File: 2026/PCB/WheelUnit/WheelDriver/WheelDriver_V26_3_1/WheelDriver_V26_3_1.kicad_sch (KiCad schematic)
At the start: 44 parts, among them J1 Conn_01x03_Socket, J10 Conn_01x04_Socket, J11 Conn_01x04_Socket, J12 Conn_01x04_Socket, J13 Conn_01x04_Socket, J14 Conn_01x06_Socket, J15 Conn_01x03_Socket, J16 Conn_01x03_Socket, J2 Conn_01x03_Socket, J9 Debug

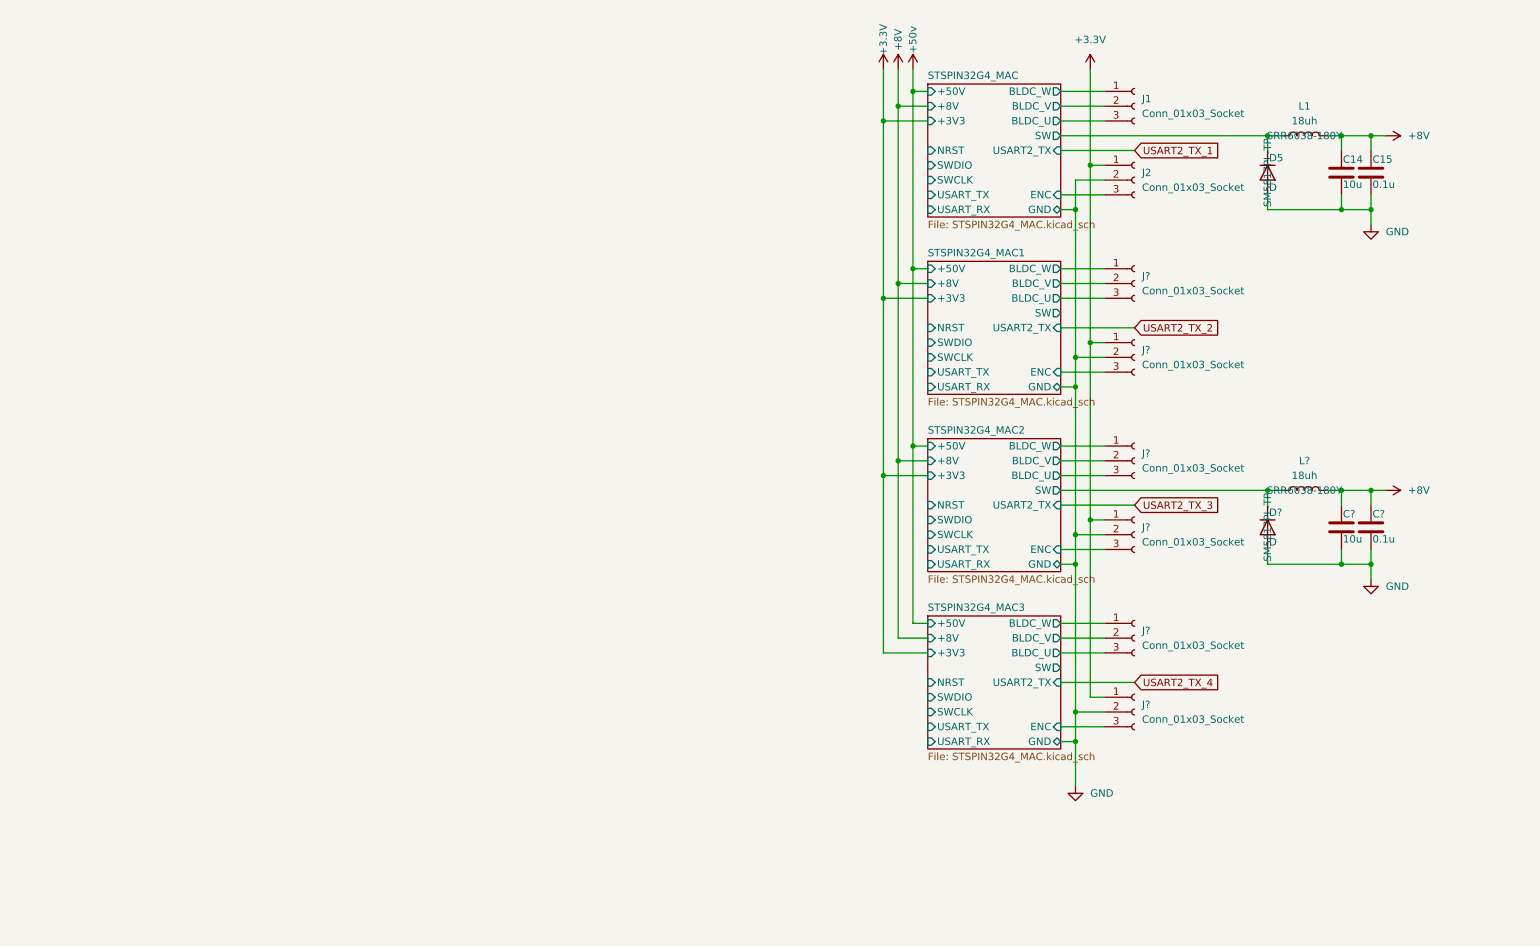
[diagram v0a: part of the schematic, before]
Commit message: 書き込み系統のバス追加
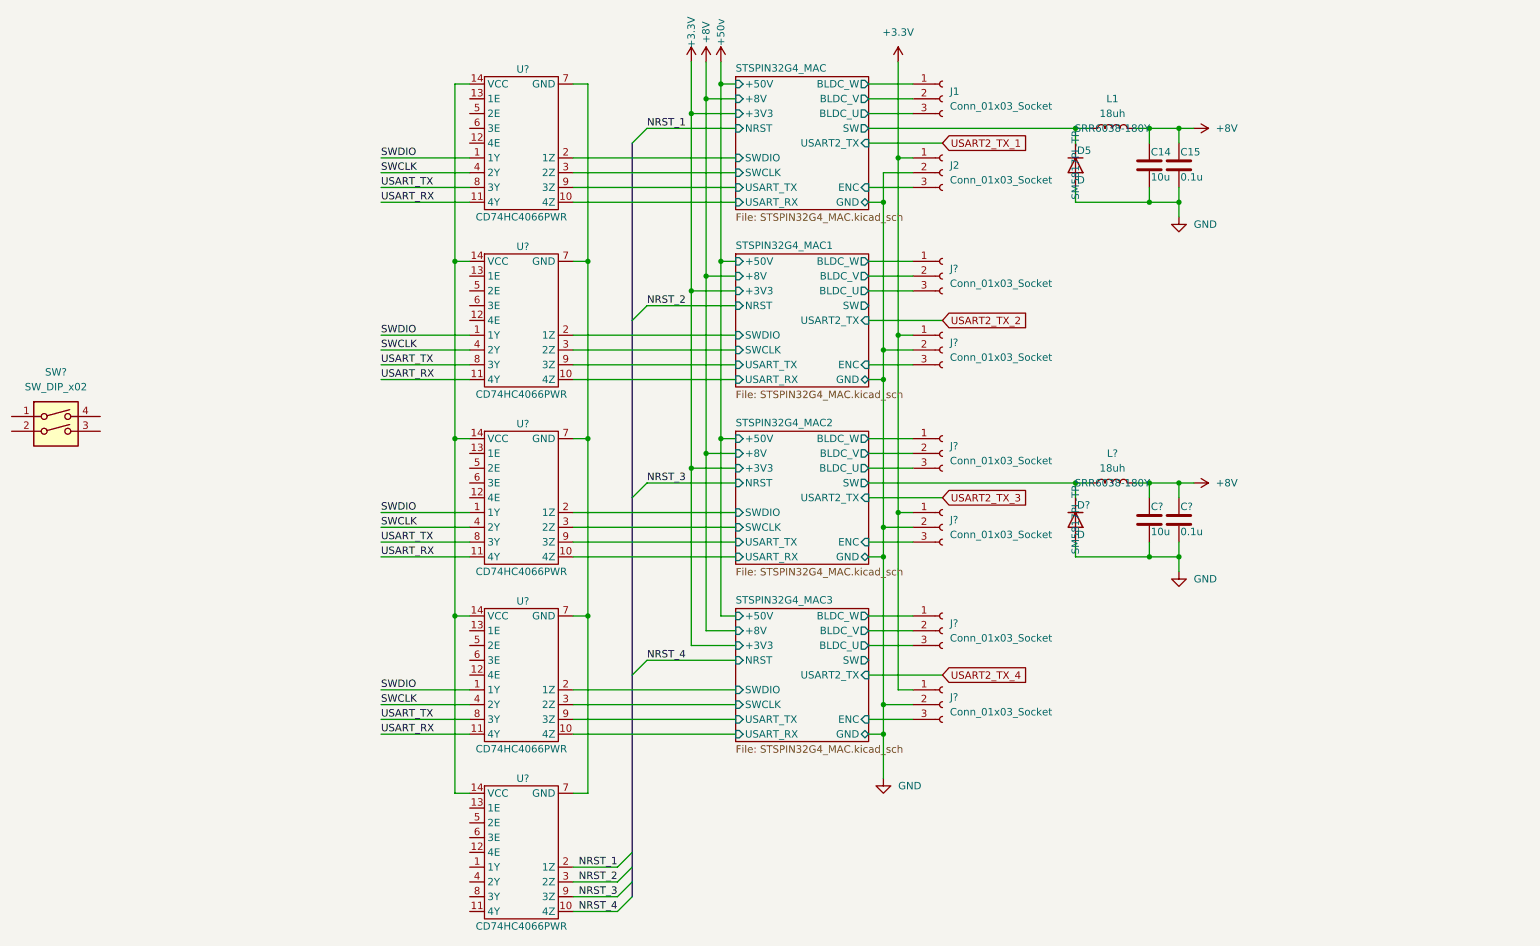
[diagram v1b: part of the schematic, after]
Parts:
- added SW?: SW_DIP_x02, symbol Switch:SW_DIP_x02
- added U? (x5): CD74HC4066PWR, symbol WheelUnit_LIB_SYM:CD74HC4066PWR
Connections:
- net STSPIN32G4_MAC/SWCLK: now also U?.3 (2Z)
- net STSPIN32G4_MAC/SWDIO: now also U?.2 (1Z)
- net STSPIN32G4_MAC/USART_RX: now also U?.10 (4Z)
- net STSPIN32G4_MAC/USART_TX: now also U?.9 (3Z)
- net STSPIN32G4_MAC1/SWCLK: now also U?.3 (2Z)
- net STSPIN32G4_MAC1/SWDIO: now also U?.2 (1Z)
- net STSPIN32G4_MAC1/USART_RX: now also U?.10 (4Z)
- net STSPIN32G4_MAC1/USART_TX: now also U?.9 (3Z)
- net STSPIN32G4_MAC2/SWCLK: now also U?.3 (2Z)
- net STSPIN32G4_MAC2/SWDIO: now also U?.2 (1Z)
- net STSPIN32G4_MAC2/USART_RX: now also U?.10 (4Z)
- net STSPIN32G4_MAC2/USART_TX: now also U?.9 (3Z)
- net STSPIN32G4_MAC3/SWCLK: now also U?.3 (2Z)
- net STSPIN32G4_MAC3/SWDIO: now also U?.2 (1Z)
- net STSPIN32G4_MAC3/USART_RX: now also U?.10 (4Z)
- net STSPIN32G4_MAC3/USART_TX: now also U?.9 (3Z)
- net SWCLK: now also U?.4 (2Y), U?.4 (2Y), U?.4 (2Y), U?.4 (2Y)
- net SWDIO: now also U?.1 (1Y), U?.1 (1Y), U?.1 (1Y), U?.1 (1Y)
- new net: U?.14 (VCC), U?.14 (VCC), U?.14 (VCC), U?.14 (VCC), U?.14 (VCC)
- new net: U?.7 (GND), U?.7 (GND), U?.7 (GND), U?.7 (GND), U?.7 (GND)
- new net NRST_1: U?.2 (1Z)
- new net NRST_2: U?.3 (2Z)
- new net NRST_3: U?.9 (3Z)
- new net NRST_4: U?.10 (4Z)
- new net USART_RX: U?.11 (4Y), U?.11 (4Y), U?.11 (4Y), U?.11 (4Y)
- new net USART_TX: U?.8 (3Y), U?.8 (3Y), U?.8 (3Y), U?.8 (3Y)
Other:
- moved on the sheet: C14, C15, C?, D5, D?, J1, J2, J?, L1, L?

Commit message: スイッチングの配線終わり
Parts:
- removed J14: Conn_01x06_Socket, Connector_JST:JST_PH_S6B-PH-K_1x06_P2.00mm_Horizontal, symbol Connector:Conn_01x06_Socket
- removed J9: Debug, Connector_JST:JST_PH_S7B-PH-K_1x07_P2.00mm_Horizontal, symbol Connector:Conn_01x07_Pin
- added J3: Conn_01x07_Pin, symbol Connector:Conn_01x07_Pin
- added J4: Conn_01x06_Pin, symbol Connector:Conn_01x06_Pin
- added SW1: SW_DIP_x02, symbol Switch:SW_DIP_x02
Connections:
- net +3.3V: now also J3.6 (Pin_6)
- net GND: now also J3.7 (Pin_7), J4.6 (Pin_6)
- net NRST: now also U?.1 (1Y), U?.11 (4Y), U?.4 (2Y), U?.8 (3Y), J3.3 (Pin_3)
- net SWCLK: now also J3.4 (Pin_4)
- net SWDIO: now also J3.5 (Pin_5)
- net USART2_RX: now also J4.5 (Pin_5)
- net USART_RX: now also J3.1 (Pin_1)
- net USART_TX: now also J3.2 (Pin_2)
- net at SW?.1: now also SW?.2, SW1.1, SW1.2
- net WRITE_SW2: now reaches SW?.3
- net WRITE_SW2: now also U?.12 (4E), U?.13 (1E), U?.5 (2E), U?.5 (2E), U?.6 (3E)
- net WRITE_SW1: now reaches SW?.4
- net WRITE_SW1: now also U?.12 (4E), U?.13 (1E), U?.13 (1E), U?.5 (2E), U?.6 (3E)
- net WRITE_SW4: now reaches U?.12 (4E)
- net WRITE_SW4: now also U?.12 (4E), U?.13 (1E), U?.5 (2E), U?.6 (3E), SW1.3
- net WRITE_SW3: now reaches U?.12 (4E)
- net WRITE_SW3: now also U?.13 (1E), U?.5 (2E), U?.6 (3E), U?.6 (3E), SW1.4
- new net USART2_TX1: J4.1 (Pin_1)
- new net USART2_TX2: J4.2 (Pin_2)
- new net USART2_TX3: J4.3 (Pin_3)
- new net USART2_TX4: J4.4 (Pin_4)
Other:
- sheet STSPIN32G4_MAC ports: added USART2_RX; removed none
- sheet STSPIN32G4_MAC1 ports: added USART2_RX; removed none
- sheet STSPIN32G4_MAC2 ports: added USART2_RX; removed none
- sheet STSPIN32G4_MAC3 ports: added USART2_RX; removed none
- moved on the sheet: C14, C15, C?, D1, D10, D17, D2, D24, D3, D31, D33, D34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

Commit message: 回路図修正終わり
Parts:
- removed J4: Conn_01x06_Pin, symbol Connector:Conn_01x06_Pin
- removed J? (x3): Conn_01x03_Socket, WheelUnit_LIB_FTP:Molex_SPOX_5268-03A_1x03_P2.50mm_Horizontal_ud, symbol Connector:Conn_01x03_Socket
- added J14: MD_UART, Connector_JST:JST_PH_S5B-PH-K_1x05_P2.00mm_Horizontal, symbol Connector:Conn_01x05_Socket
- added J4: BLDC2, WheelUnit_LIB_FTP:Molex_SPOX_5268-03A_1x03_P2.50mm_Horizontal_ud, symbol Connector:Conn_01x03_Socket
- added J6: BLDC3, WheelUnit_LIB_FTP:Molex_SPOX_5268-03A_1x03_P2.50mm_Horizontal_ud, symbol Connector:Conn_01x03_Socket
- added J8: BLDC4, WheelUnit_LIB_FTP:Molex_SPOX_5268-03A_1x03_P2.50mm_Horizontal_ud, symbol Connector:Conn_01x03_Socket
- J1: value Conn_01x03_Socket -> BLDC1
- J10, J11: value Conn_01x04_Socket -> PCO_GND
- J12, J13: value Conn_01x04_Socket -> PCO_50V
- J15, J16: value Conn_01x03_Socket -> PCO_3V3
- J2: value Conn_01x03_Socket -> ENC1
- J3: value Conn_01x07_Pin -> WRITE_CO; footprint (none) -> Connector_JST:JST_PH_S7B-PH-K_1x07_P2.00mm_Horizontal
- J5: renamed from J?; value Conn_01x03_Socket -> ENC2
- J7: renamed from J?; value Conn_01x03_Socket -> ENC3
- J9: renamed from J?; value Conn_01x03_Socket -> ENC4
- SW1: footprint (none) -> WheelUnit_LIB_FTP:CFS0201TB
- SW2: renamed from SW?; footprint (none) -> WheelUnit_LIB_FTP:CFS0201TB
- U1, U2, U3, U4, U5: renamed from U?; footprint (none) -> Package_SO:TSSOP-14_4.4x5mm_P0.65mm
- gave numbers to parts that had none: 4
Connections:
- net USART2_TX_1 is gone; now on net USART2_TX1: R20.1
- net USART2_TX_2 is gone; now on net USART2_TX2: R37.1
- net USART2_TX_3 is gone; now on net USART2_TX3: R40.1
- net USART2_TX_4 is gone; now on net USART2_TX4: R57.1
- net +3.3V: now also SW1.1, SW1.2, SW2.1, SW2.2, U1.14 (VCC), U2.14 (VCC), U3.14 (VCC), U4.14 (VCC), U5.14 (VCC)
- net GND: now also U1.7 (GND), U2.7 (GND), U3.7 (GND), U4.7 (GND), U5.7 (GND)
- net STSPIN32G4_MAC1/BLDC_U: now also J4.3 (Pin_3)
- net STSPIN32G4_MAC1/BLDC_V: now also J4.2 (Pin_2)
- net STSPIN32G4_MAC1/BLDC_W: now also J4.1 (Pin_1)
- net STSPIN32G4_MAC2/BLDC_U: now also J6.3 (Pin_3)
- net STSPIN32G4_MAC2/BLDC_V: now also J6.2 (Pin_2)
- net STSPIN32G4_MAC2/BLDC_W: now also J6.1 (Pin_1)
- net STSPIN32G4_MAC3/BLDC_U: now also J8.3 (Pin_3)
- net STSPIN32G4_MAC3/BLDC_V: now also J8.2 (Pin_2)
- net STSPIN32G4_MAC3/BLDC_W: now also J8.1 (Pin_1)
- net USART2_RX: now also J14.5 (Pin_5)
- net USART2_TX1: now also J14.1 (Pin_1)
- net USART2_TX2: now also J14.2 (Pin_2)
- net USART2_TX3: now also J14.3 (Pin_3)
- net USART2_TX4: now also J14.4 (Pin_4)
- net USART_RX: no longer U1.11 (4Y), U2.11 (4Y), U3.11 (4Y), U4.11 (4Y)
- net USART_TX: no longer U1.8 (3Y), U2.8 (3Y), U3.8 (3Y), U4.8 (3Y)
- net UART1_RX renamed USART1_RX
- net USART1_RX: now also U1.11 (4Y), U2.11 (4Y), U3.11 (4Y), U4.11 (4Y)
- net UART1_TX renamed USART1_TX
- net USART1_TX: now also U1.8 (3Y), U2.8 (3Y), U3.8 (3Y), U4.8 (3Y)
- no-connect marks 0 -> 2
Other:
- moved on the sheet: C1, C14, C15, C2, D1, D10, D17, D2, D24, D3, D31, D33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

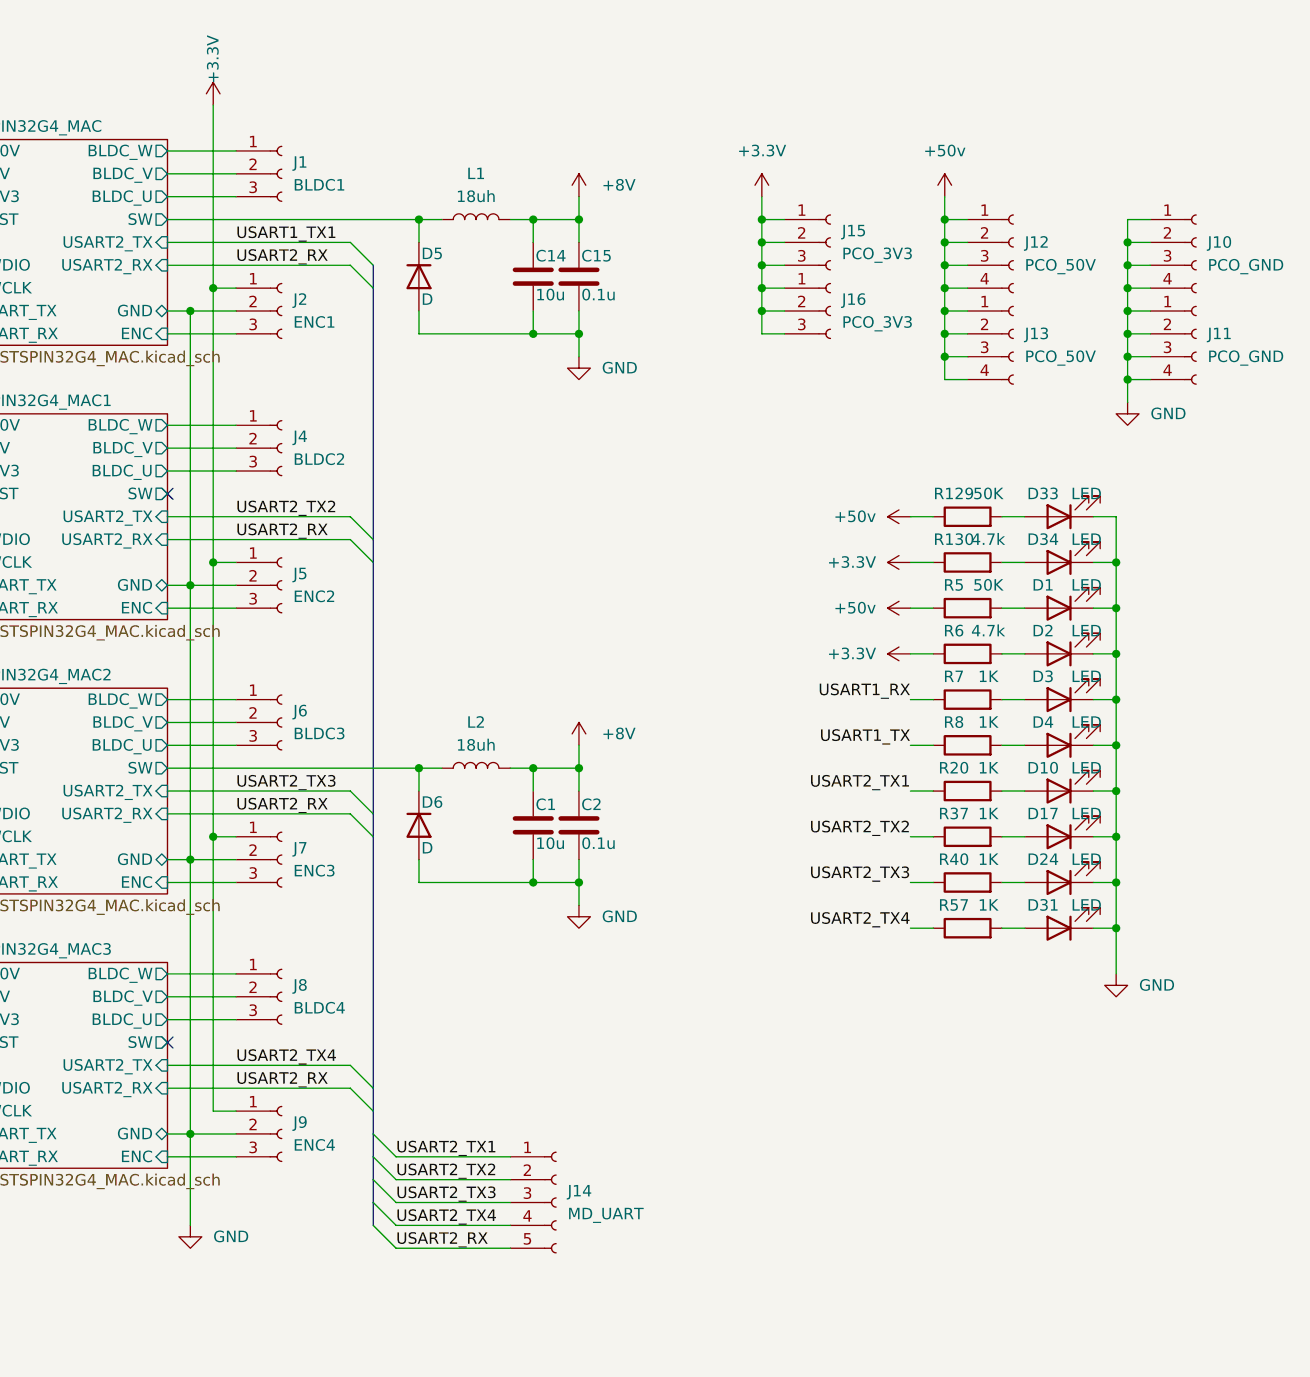
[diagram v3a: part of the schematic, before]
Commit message: 部品配置終わり
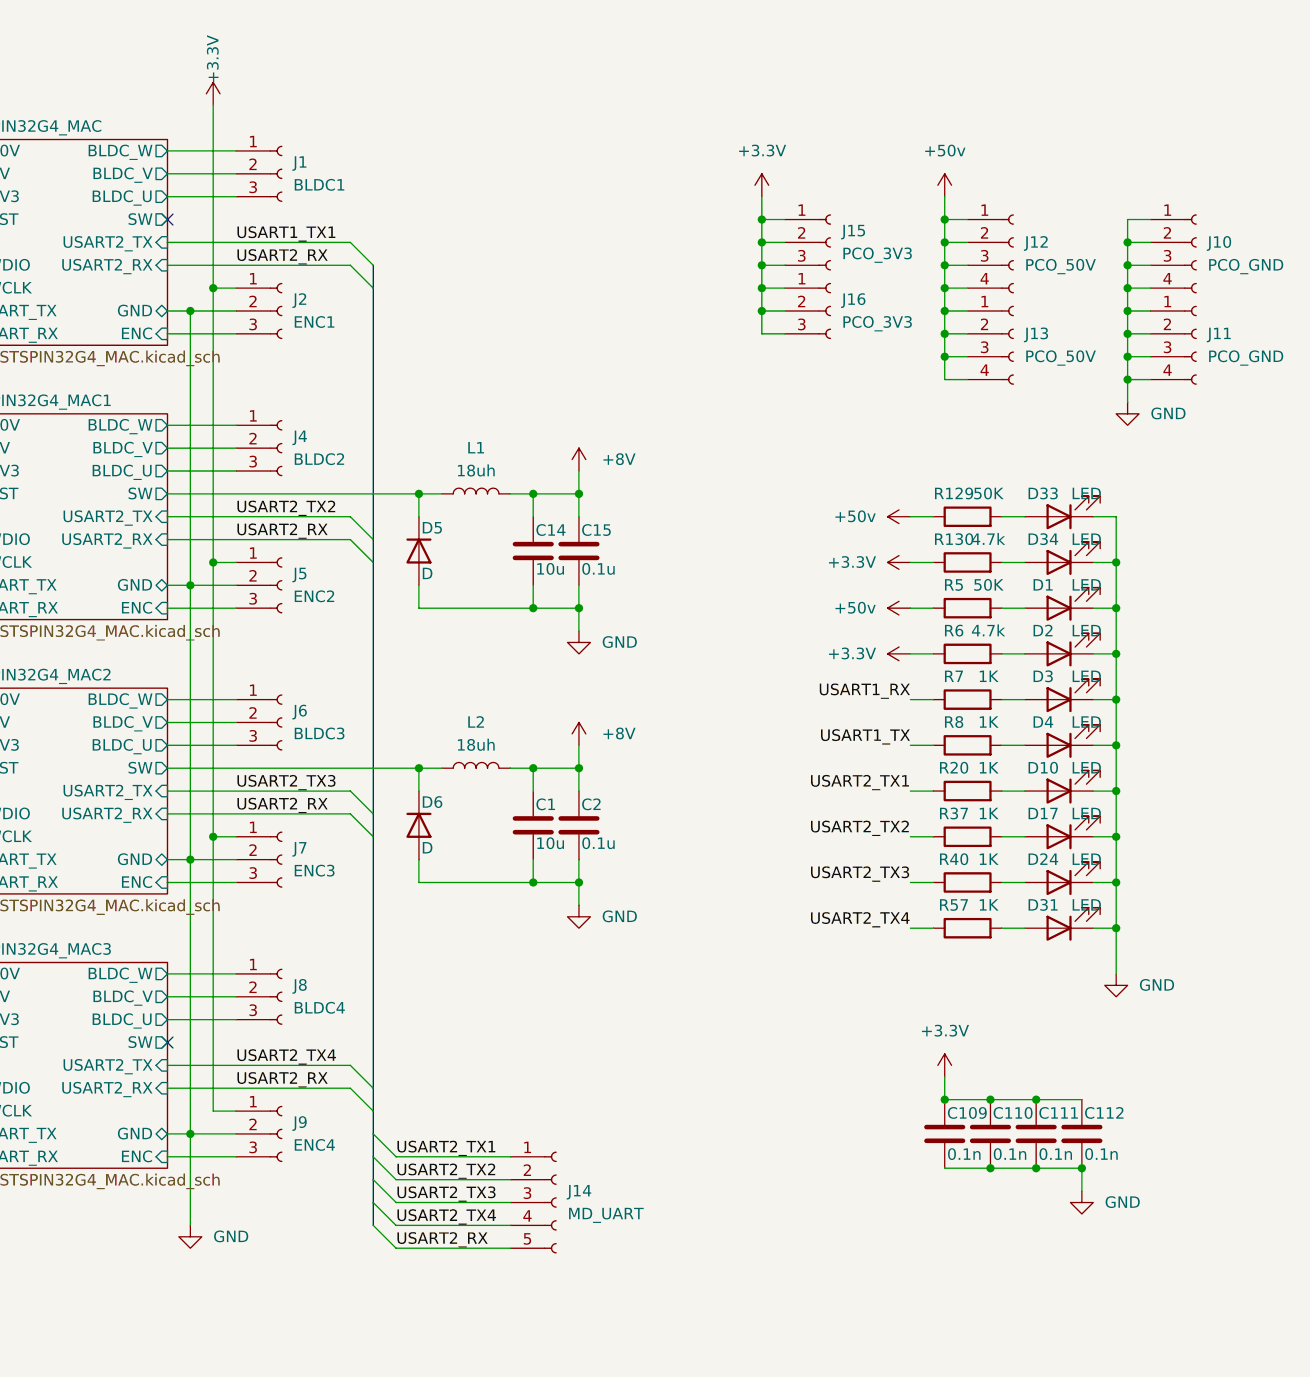
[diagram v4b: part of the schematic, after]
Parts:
- added C109, C110, C111, C112: 0.1n, Capacitor_SMD:C_0603_1608Metric_Pad1.08x0.95mm_HandSolder, symbol Device:C
- R20, R37, R40, R57, R7, R8: footprint Resistor_SMD:R_0402_1005Metric_Pad0.72x0.64mm_HandSolder -> Resistor_SMD:R_0603_1608Metric_Pad0.98x0.95mm_HandSolder
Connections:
- net +3.3V: now also C109.1, C110.1, C111.1, C112.1
- net GND: now also C109.2, C110.2, C111.2, C112.2
- net STSPIN32G4_MAC/SW: no longer D5.1 (K), L1.1
- net STSPIN32G4_MAC1/SW: now also D5.1 (K), L1.1
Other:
- moved on the sheet: C14, C15, D5, L1

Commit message: 配線途中 =^.^= !!!!!????
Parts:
- added D37, D38: LED, WheelUnit_LIB_FTP:LED_1608_user_dif, symbol Device:LED
- added R121, R122: 10k, Resistor_SMD:R_0603_1608Metric_Pad0.98x0.95mm_HandSolder, symbol Device:R
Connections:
- net USART_RX is gone; now on net USART1_RX: J3.1 (Pin_1)
- net USART_TX is gone; now on net USART1_TX: J3.2 (Pin_2)
- net +8V: now also R121.1, R122.1
- net GND: now also D37.1 (K), D38.1 (K)
- new net: D37.2 (A), R121.2
- new net: D38.2 (A), R122.2
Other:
- moved on the sheet: J10, J11, J12, J13, J15, J16

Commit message: 設計終わり
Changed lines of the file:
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@@
 		)
 	)
-	(label "USART1_TX1"
+	(label "USART2_TX1"
 		(at 163.83 43.18 0)
 		(effects
